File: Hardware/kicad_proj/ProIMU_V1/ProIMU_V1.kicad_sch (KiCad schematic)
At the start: 20 parts, among them U1 BMP280, U2 MPU-9250, U3 STM32F412CEU6

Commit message: Updated Hardware Files
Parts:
- removed J?: USB_C_Receptacle_USB2.0, symbol Connector:USB_C_Receptacle_USB2.0
- added C?: 100nF, symbol Device:C_Small
- added J?: 502570-0893, MOLEX_502570-0893, symbol 502570-0893:502570-0893
- added J?: USB4105-GF-A, GCT_USB4105-GF-A, symbol USB4105-GF-A:USB4105-GF-A
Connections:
- net +3V3: now also C?.2, J?.4 (VDD)
- net +5V: now also J?.A4_B9 (VBUS), J?.B4_A9 (VBUS)
- net GND: now also C?.1, J?.6 (VSS), J?.A1_B12 (GND), J?.B1_A12 (GND)
- net SDACRD_DET_SWT: now also J?.DS (DET_SWT)
- net SDCARD_CLK: now also J?.5 (CLK)
- net SDCARD_CMD: now also J?.3 (CMD)
- net SDCARD_D0: now also J?.7 (DAT0)
- net SDCARD_D1: now also J?.8 (DAT1)
- net SDCARD_D2: now also J?.1 (DAT2)
- net SDCARD_D3: now also J?.2 (CD/DAT3)
- net SDCARD_DET_LEVEL: now also J?.DL (DET_LEVEL)
- net USB+: now also J?.A6 (DP1), J?.B6 (DP2)
- net USB-: now also J?.A7 (DN1), J?.B7 (DN2)
- new net: J?.S1 (SHELL_GND), J?.S2 (SHELL_GND), J?.S3 (SHELL_GND), J?.S4 (SHELL_GND)
- no-connect marks 19 -> 24
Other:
- note added: "Micro SD Card"
- moved on the sheet: BAT1, C1, C3, C4, C5, C6, C7, C8, PWR1, R3, SWD1, U1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

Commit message: 09-02-2022 Hardware Update
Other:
- note added: "BATTERY CHARGER MODULE DC-DC CONVERTER WIFI/BLE MODEM CRYSTAL CIRCUIT MOUNTING HOLES GPS"
- note removed: "BATTERY CHARGER MODULE DC-DC CONVERTER WIFI/BLE MODEM CRYSTAL CIRCUIT SD CARD MOUNTING HOLES GPS"
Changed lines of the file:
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@@
     (effects (font (size 1.27 1.27)) (justify left bottom))
   )
-  (text "BATTERY CHARGER MODULE\nDC-DC CONVERTER\nWIFI/BLE MODEM\nCRYSTAL CIRCUIT\nSD CARD\nMOUNTING HOLES\nGPS"
+  (text "BATTERY CHARGER MODULE\nDC-DC CONVERTER\nWIFI/BLE MODEM\nCRYSTAL CIRCUIT\nMOUNTING HOLES\nGPS"
     (at 109.22 -10.16 0)
     (effects (font (size 1.27 1.27)) (justify left bottom))

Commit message: Update: Hardware Files. Added Air602 Module
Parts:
- added U?: AIR602, symbol air602:AIR602
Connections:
- net +3V3: now also U?.4 (VCC)
- net GND: now also U?.1 (GND), U?.3 (GND)
- net WIFI_UART_RX: now also U?.5 (TX0)
- net WIFI_UART_TX: now also U?.6 (RX0)
- net WIFI_RES: now reaches U3.14 (PA4)
- net WIFI_RES: now also U?.12 (RES)
- new net ANT: U?.2 (ANT)
- no-connect marks 24 -> 28
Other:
- note added: "WiFi:"
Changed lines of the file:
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@@
   (no_connect (at 207.01 68.58))
   (no_connect (at 207.01 27.94))
-  (no_connect (at 207.01 35.56))
   (no_connect (at 207.01 38.1))
   (no_connect (at 207.01 43.18))
@@
   (no_connect (at 265.43 38.1))
   (no_connect (at 80.01 109.22))
+  (no_connect (at 138.43 95.885))
+  (no_connect (at 138.43 98.425))
+  (no_connect (at 138.43 93.345))
+  (no_connect (at 138.43 90.805))
+  (no_connect (at 138.43 88.265))
   (no_connect (at 48.26 96.52))
   (no_connect (at 96.52 178.435))
@@
     (stroke (width 0) (type default) (color 0 0 0 0))
   )
+  (polyline (pts (xy 107.315 113.665) (xy 153.67 113.665))
+    (stroke (width 0) (type default) (color 0 0 0 0))
+  )
   (wire (pts (xy 198.12 55.88) (xy 207.01 55.88))
     (stroke (width 0) (type default) (color 0 0 0 0))
@@
     (stroke (width 0) (type default) (color 0 0 0 0))
   )
+  (polyline (pts (xy 107.315 111.125) (xy 107.315 113.665))
+    (stroke (width 0) (type default) (color 0 0 0 0))
+  )
+  (wire (pts (xy 115.57 93.345) (xy 118.11 93.345))
+    (stroke (width 0) (type default) (color 0 0 0 0))
+  )
   (polyline (pts (xy 12.7 132.08) (xy 106.68 132.08))
     (stroke (width 0) (type default) (color 0 0 0 0))
@@
     (stroke (width 0) (type default) (color 0 0 0 0))
   )
+  (wire (pts (xy 138.43 83.185) (xy 140.335 83.185))
+    (stroke (width 0) (type default) (color 0 0 0 0))
+  )
   (wire (pts (xy 128.27 27.94) (xy 129.54 27.94))
     (stroke (width 0) (type default) (color 0 0 0 0))
@@
     (stroke (width 0) (type default) (color 0 0 0 0))
   )
+  (polyline (pts (xy 153.67 70.485) (xy 153.67 110.49))
+    (stroke (width 0) (type default) (color 0 0 0 0))
+  )
   (wire (pts (xy 196.85 83.82) (xy 207.01 83.82))
     (stroke (width 0) (type default) (color 0 0 0 0))
@@
     (stroke (width 0) (type default) (color 0 0 0 0))
   )
+  (wire (pts (xy 118.11 77.47) (xy 118.11 83.185))
+    (stroke (width 0) (type default) (color 0 0 0 0))
+  )
   (wire (pts (xy 196.85 78.74) (xy 207.01 78.74))
     (stroke (width 0) (type default) (color 0 0 0 0))
@@
     (stroke (width 0) (type default) (color 0 0 0 0))
   )
+  (polyline (pts (xy 154.305 12.7) (xy 177.165 12.7))
+    (stroke (width 0) (type default) (color 0 0 0 0))
+  )
   (wire (pts (xy 198.12 63.5) (xy 207.01 63.5))
     (stroke (width 0) (type default) (color 0 0 0 0))
@@
     (stroke (width 0) (type default) (color 0 0 0 0))
   )
+  (polyline (pts (xy 153.67 113.665) (xy 153.67 110.49))
+    (stroke (width 0) (type default) (color 0 0 0 0))
+  )
   (wire (pts (xy 127.635 22.86) (xy 129.54 22.86))
     (stroke (width 0) (type default) (color 0 0 0 0))
@@
     (stroke (width 0) (type default) (color 0 0 0 0))
   )
+  (polyline (pts (xy 107.315 110.49) (xy 153.67 110.49))
+    (stroke (width 0) (type default) (color 0 0 0 0))
+  )
+  (polyline (pts (xy 154.305 12.7) (xy 154.305 22.225))
+    (stroke (width 0) (type default) (color 0 0 0 0))
+  )
   (polyline (pts (xy 12.7 12.7) (xy 12.7 62.23))
     (stroke (width 0) (type default) (color 0 0 0 0))
@@
     (stroke (width 0) (type default) (color 0 0 0 0))
   )
+  (wire (pts (xy 118.11 98.425) (xy 118.11 104.14))
+    (stroke (width 0) (type default) (color 0 0 0 0))
+  )
   (polyline (pts (xy 107.315 17.145) (xy 107.315 66.04))
     (stroke (width 0) (type default) (color 0 0 0 0))
@@
     (stroke (width 0) (type default) (color 0 0 0 0))
   )
+  (polyline (pts (xy 177.165 12.7) (xy 177.165 16.51))
+    (stroke (width 0) (type default) (color 0 0 0 0))
+  )
   (wire (pts (xy 91.44 91.44) (xy 91.44 76.2))
     (stroke (width 0) (type default) (color 0 0 0 0))
@@
     (stroke (width 0) (type default) (color 0 0 0 0))
   )
+  (wire (pts (xy 198.12 35.56) (xy 207.01 35.56))
+    (stroke (width 0) (type default) (color 0 0 0 0))
+  )
   (wire (pts (xy 33.02 177.8) (xy 33.02 172.72))
     (stroke (width 0) (type default) (color 0 0 0 0))
@@
     (stroke (width 0) (type default) (color 0 0 0 0))
   )
+  (wire (pts (xy 116.205 88.265) (xy 118.11 88.265))
+    (stroke (width 0) (type default) (color 0 0 0 0))
+  )
   (wire (pts (xy 80.01 25.4) (xy 77.47 25.4))
     (stroke (width 0) (type default) (color 0 0 0 0))
@@
     (stroke (width 0) (type default) (color 0 0 0 0))
   )
+  (polyline (pts (xy 153.67 70.485) (xy 107.315 70.485))
+    (stroke (width 0) (type default) (color 0 0 0 0))
+  )
   (wire (pts (xy 27.94 44.45) (xy 30.48 44.45))
     (stroke (width 0) (type default) (color 0 0 0 0))
@@
     (stroke (width 0) (type default) (color 0 0 0 0))
   )
+  (polyline (pts (xy 107.315 70.485) (xy 107.315 110.49))
+    (stroke (width 0) (type default) (color 0 0 0 0))
+  )
   (wire (pts (xy 196.85 104.14) (xy 207.01 104.14))
     (stroke (width 0) (type default) (color 0 0 0 0))
@@
   )
   (wire (pts (xy 35.56 38.1) (xy 35.56 46.99))
+    (stroke (width 0) (type default) (color 0 0 0 0))
+  )
+  (wire (pts (xy 138.43 85.725) (xy 140.335 85.725))
     (stroke (width 0) (type default) (color 0 0 0 0))
   )
@@
     (effects (font (size 1.27 1.27)) (justify left bottom))
   )
+  (text "WiFi:" (at 107.95 113.03 0)
+    (effects (font (size 1.27 1.27)) (justify left bottom))
+  )
   (text "MPU9250: Inertial Measurement Unit" (at 13.97 130.81 0)
     (effects (font (size 1.27 1.27)) (justify left bottom))
@@
   )
   (text "BATTERY CHARGER MODULE\nDC-DC CONVERTER\nWIFI/BLE MODEM\nCRYSTAL CIRCUIT\nMOUNTING HOLES\nGPS"
-    (at 109.22 -10.16 0)
+    (at 113.665 6.35 0)
     (effects (font (size 1.27 1.27)) (justify left bottom))
   )
@@
     (effects (font (size 1.27 1.27)) (justify left bottom))
   )
+  (label "WIFI_RES" (at 198.12 35.56 180)
+    (effects (font (size 1.27 1.27)) (justify right bottom))
+  )
   (label "SDACRD_DET_SWT" (at 128.27 40.64 180)
     (effects (font (size 1.27 1.27)) (justify right bottom))
@@
     (effects (font (size 1.27 1.27)) (justify right bottom))
   )
+  (label "WIFI_UART_TX" (at 140.335 85.725 0)
+    (effects (font (size 1.27 1.27)) (justify left bottom))
+  )
   (label "SDCARD_D2" (at 128.27 35.56 180)
     (effects (font (size 1.27 1.27)) (justify right bottom))
@@
     (effects (font (size 1.27 1.27)) (justify right bottom))
   )
+  (label "WIFI_UART_RX" (at 140.335 83.185 0)
+    (effects (font (size 1.27 1.27)) (justify left bottom))
+  )
   (label "NRST" (at 265.424 43.18 0)
     (effects (font (size 1.27 1.27)) (justify left bottom))
@@
     (effects (font (size 1.27 1.27)) (justify right bottom))
   )
+  (label "ANT" (at 115.57 93.345 180)
+    (effects (font (size 1.27 1.27)) (justify right bottom))
+  )
   (label "SDCARD_DET_LEVEL" (at 128.27 43.18 180)
     (effects (font (size 1.27 1.27)) (justify right bottom))
@@
   )
   (label "MPU9250_SCL" (at 196.85 83.82 180)
+    (effects (font (size 1.27 1.27)) (justify right bottom))
+  )
+  (label "WIFI_RES" (at 116.205 88.265 180)
     (effects (font (size 1.27 1.27)) (justify right bottom))
   )
@@
     (pin "1")
   )
+  (symbol (lib_id "power:GND") (at 118.11 104.14 0) (unit 1)
+    (in_bom yes) (on_board yes) (fields_autoplaced)
+    (property "Reference" "#PWR?" (id 0) (at 118.11 110.49 0)
+      (effects (font (size 1.27 1.27)) hide)
+    )
+    (property "Value" "GND" (id 1) (at 118.11 109.22 0))
+    (property "Footprint" "" (id 2) (at 118.11 104.14 0)
+      (effects (font (size 1.27 1.27)) hide)
+    )
+    (property "Datasheet" "" (id 3) (at 118.11 104.14 0)
+      (effects (font (size 1.27 1.27)) hide)
+    )
+    (pin "1")
+  )
   (symbol (lib_id "power:+5V") (at 78.74 139.065 270) (unit 1)
     (in_bom yes) (on_board yes) (fields_autoplaced)
@@
     (pin "2")
   )
+  (symbol (lib_id "power:+3V3") (at 118.11 77.47 0) (unit 1)
+    (in_bom yes) (on_board yes) (fields_autoplaced)
+    (property "Reference" "#PWR?" (id 0) (at 118.11 81.28 0)
+      (effects (font (size 1.27 1.27)) hide)
+    )
+    (property "Value" "+3V3" (id 1) (at 118.11 71.755 0))
+    (property "Footprint" "" (id 2) (at 118.11 77.47 0)
+      (effects (font (size 1.27 1.27)) hide)
+    )
+    (property "Datasheet" "" (id 3) (at 118.11 77.47 0)
+      (effects (font (size 1.27 1.27)) hide)
+    )
+    (pin "1")
+  )
   (symbol (lib_id "power:+5V") (at 34.29 139.7 270) (unit 1)
     (in_bom yes) (on_board yes) (fields_autoplaced)
@@
     )
     (pin "1")
+  )
+  (symbol (lib_id "air602:AIR602") (at 128.27 90.805 0) (unit 1)
+    (in_bom yes) (on_board yes) (fields_autoplaced)
+    (property "Reference" "U?" (id 0) (at 128.27 74.93 0))
+    (property "Value" "AIR602" (id 1) (at 128.27 77.47 0))
+    (property "Footprint" "" (id 2) (at 128.27 90.805 0)
+      (effects (font (size 1.27 1.27)) hide)
+    )
+    (property "Datasheet" "" (id 3) (at 128.27 90.805 0)
+      (effects (font (size 1.27 1.27)) hide)
+    )
+    (pin "1")
+    (pin "10")
+    (pin "11")
+    (pin "12")
+    (pin "2")
+    (pin "3")
+    (pin "4")
+    (pin "5")
+    (pin "6")
+    (pin "7")
+    (pin "8")
+    (pin "9")
   )
   (symbol (lib_id "USB4105-GF-A:USB4105-GF-A") (at 76.2 175.895 0) (unit 1)
@@
       (reference "#PWR?") (unit 1) (value "+5V") (footprint "")
     )
+    (path "/d0f23bb4-6998-469d-9c0a-2c687b63ad14"
+      (reference "#PWR?") (unit 1) (value "GND") (footprint "")
+    )
+    (path "/d9a7475e-cc92-46fe-b86c-51c1b85bc3aa"
+      (reference "#PWR?") (unit 1) (value "+3V3") (footprint "")
+    )
     (path "/f2993afa-8b01-4f65-9da6-9195c8afc0c0"
       (reference "#PWR?") (unit 1) (value "+3V3") (footprint "")
@@
       (reference "U3") (unit 2) (value "STM32F412CEU6") (footprint "footprints:QFN50P700X700X60-49N")
     )
-  )
+    (path "/dc13530d-fe62-4a26-9917-28e91f6b38c5"
+      (reference "U?") (unit 1) (value "AIR602") (footprint "")
+    )
+  )

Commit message: Update: Added Mounting Holes to the schematic
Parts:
- added H? (x4): MountingHole, symbol Mechanical:MountingHole
- gave numbers to parts that had none: 4
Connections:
- net GND: now also J1.S1 (SHELL_GND), J1.S2 (SHELL_GND), J1.S3 (SHELL_GND), J1.S4 (SHELL_GND)
- no-connect marks 28 -> 27
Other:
- note added: "3.2 mm Holes"
- note added: "BATTERY CHARGER MODULE DC-DC CONVERTER CRYSTAL CIRCUIT GPS"
- note removed: "BATTERY CHARGER MODULE DC-DC CONVERTER WIFI/BLE MODEM CRYSTAL CIRCUIT MOUNTING HOLES GPS"
- moved on the sheet: C2, R5, U3A, U3B

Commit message: Update: Schematic. Linked 3D models to footprints
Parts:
- J2: footprint MOLEX_502570-0893 -> footprints:MOLEX_502570-0893
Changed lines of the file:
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@@
     (property "Reference" "J2" (id 0) (at 142.24 17.145 0))
     (property "Value" "502570-0893" (id 1) (at 142.24 19.05 0))
-    (property "Footprint" "MOLEX_502570-0893" (id 2) (at 147.32 33.02 0)
+    (property "Footprint" "footprints:MOLEX_502570-0893" (id 2) (at 147.32 33.02 0)
       (effects (font (size 1.27 1.27)) (justify left bottom) hide)
     )
@@
     )
     (path "/6e3ff496-d404-4c22-8d76-cfb864912843"
-      (reference "J2") (unit 1) (value "502570-0893") (footprint "MOLEX_502570-0893")
+      (reference "J2") (unit 1) (value "502570-0893") (footprint "footprints:MOLEX_502570-0893")
     )
     (path "/ef4db96a-f7d7-4a70-8c0a-4ef685b27e8d"

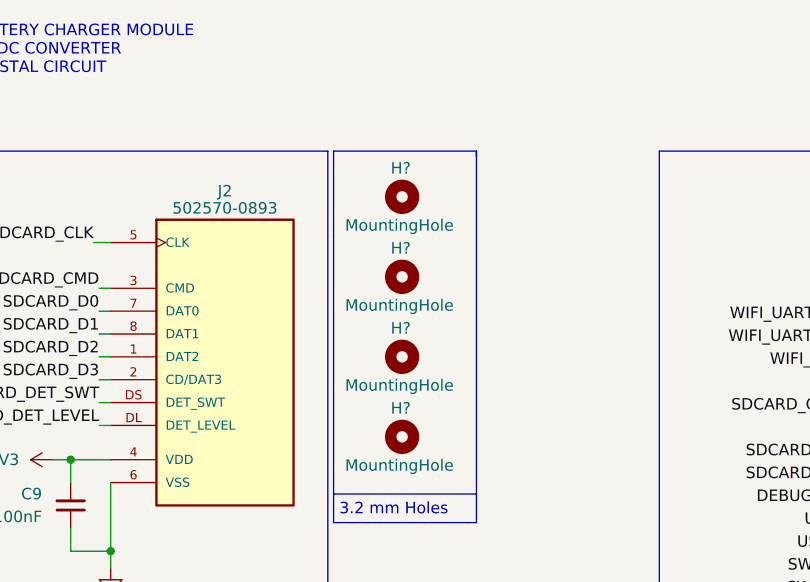
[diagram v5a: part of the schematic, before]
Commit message: Udate: Schematic | Added: Footprint allocation for symbols
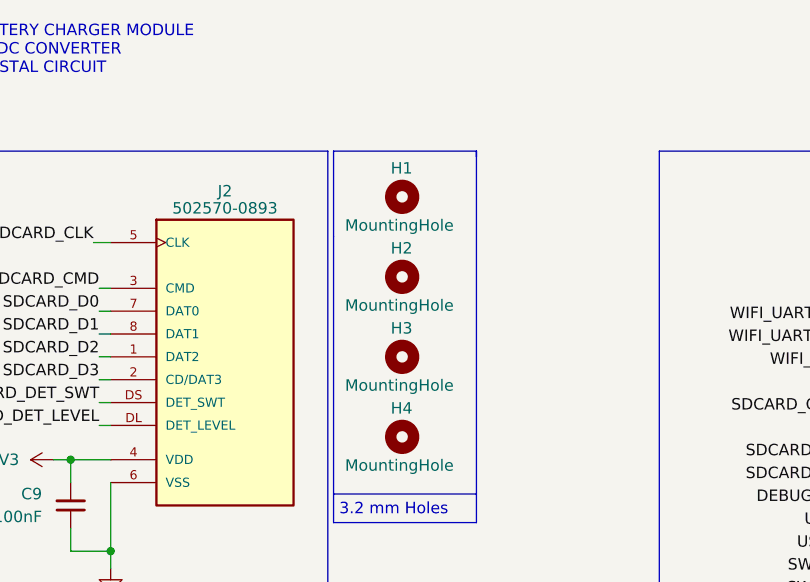
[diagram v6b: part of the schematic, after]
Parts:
- BAT1: footprint (none) -> Connector_PinSocket_2.54mm:PinSocket_1x02_P2.54mm_Vertical
- C1, C2, C3, C4, C5, C6, C7, C8, C9: footprint (none) -> Capacitor_SMD:C_0402_1005Metric_Pad0.74x0.62mm_HandSolder
- H1, H2, H3, H4: renamed from H?; footprint (none) -> MountingHole:MountingHole_2.2mm_M2
- J1: footprint GCT_USB4105-GF-A -> footprints:GCT_USB4105-GF-A
- PWR1, SWD1: footprint (none) -> Connector_PinSocket_2.54mm:PinSocket_2x03_P2.54mm_Vertical
- R1, R2, R3, R4, R5: footprint (none) -> Resistor_SMD:R_0402_1005Metric_Pad0.72x0.64mm_HandSolder
- U1: footprint LGA8_BMP280_BOS -> footprints:BMP280
- U2: footprint QFN40P300X300X105-24N -> footprints:QFN40P300X300X105-24N
- U4: footprint (none) -> footprints:AIR602

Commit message: Update: PCB Layout
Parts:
- removed PWR1, SWD1: Conn_02x03_Counter_Clockwise, Connector_PinSocket_2.54mm:PinSocket_2x03_P2.54mm_Vertical, symbol Connector_Generic:Conn_02x03_Counter_Clockwise
- added COMMS1: Conn_01x06, Connector_JST:JST_XH_S6B-XH-A-1_1x06_P2.50mm_Horizontal, symbol Connector_Generic:Conn_01x06
- added U5, U6, U7, U8, U9: POGOPIN, footprints:1.27MM_POGO, symbol POGOPIN:POGOPIN
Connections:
- net +5V: now also COMMS1.1 (Pin_1), U9.P$1
- net CAN_TRX+: now also COMMS1.3 (Pin_3)
- net CAN_TRX-: now also COMMS1.2 (Pin_2)
- net GND: now also COMMS1.6 (Pin_6), U8.P$1
- net NRST: now also U7.P$1
- net SWCLK: now also U5.P$1
- net SWDIO: now also U6.P$1
- net UART_RX: now also COMMS1.5 (Pin_5)
- net UART_TX: now also COMMS1.4 (Pin_4)
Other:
- moved on the sheet: C1, C8
